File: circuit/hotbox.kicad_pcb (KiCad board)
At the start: 2 copper layers, 59.7 x 26.7 mm, 35 parts, among them IC1 M48, K1 CONN_3, P1 CONN_2, P2 CONN_5, P3 CONN_4, P4 CONN_3X2, U1 REG, U2 OPTO-TRIAC, U3 BTA312Y-600C, U4 OPTO-TRANS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

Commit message: Alpha version of complete pcb, untested.
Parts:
- added 1PIN: P***, Connect:1pin, F.Cu at (87.6, 151.8)
- added 1PIN: P***, Connect:1pin, F.Cu at (139.1, 158.8)
- added 1PIN: P***, Connect:1pin, F.Cu at (139.1, 137.8)
- moved D1 3.81 mm to (85.7, 156.2)
- moved D2 2.54 mm to (85.7, 158.1)
- moved R5 2.54 mm to (92.1, 151.8), turned to 90 degrees
- moved R12 1.91 mm to (89.5, 160.0)
- moved D4 1.27 mm to (85.7, 160.0)
- moved R6 1.27 mm to (89.5, 156.2)
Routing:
- net Net-(D1-Pad1): track 2.32 -> 7.47 mm
- net /load: track 26.2 -> 21.9 mm
- net GND: track 149.3 -> 147.5 mm, vias 13 -> 12
- net Net-(IC1-Pad9): track 25.6 -> 24.3 mm
- net Net-(IC1-Pad1): track 16.7 -> 15.4 mm
- net Net-(D4-Pad1): track 2.32 -> 3.33 mm
- net +3.3V: track 90.9 -> 91.6 mm
- net Net-(D2-Pad1): track 2.32 -> 2.85 mm
- added copper zone on F.Cu, net GND
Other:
- board size 59.7 x 26.7 mm -> 59.7 x 27.7 mm
- board text added: "Hotbox v1.0 J. Villemaire-Krajden http://j-vk.com"

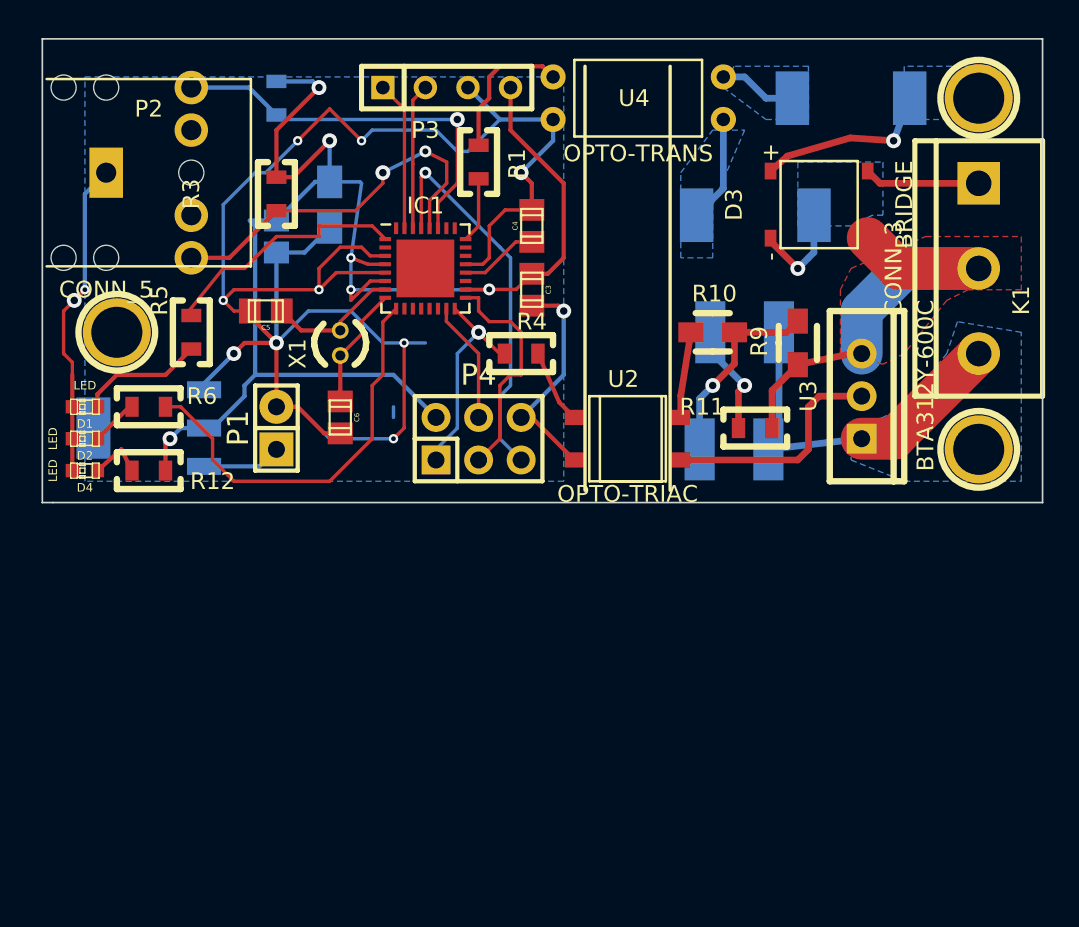
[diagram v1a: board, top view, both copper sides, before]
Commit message: Switched to 5x5cm for seeedstudio.
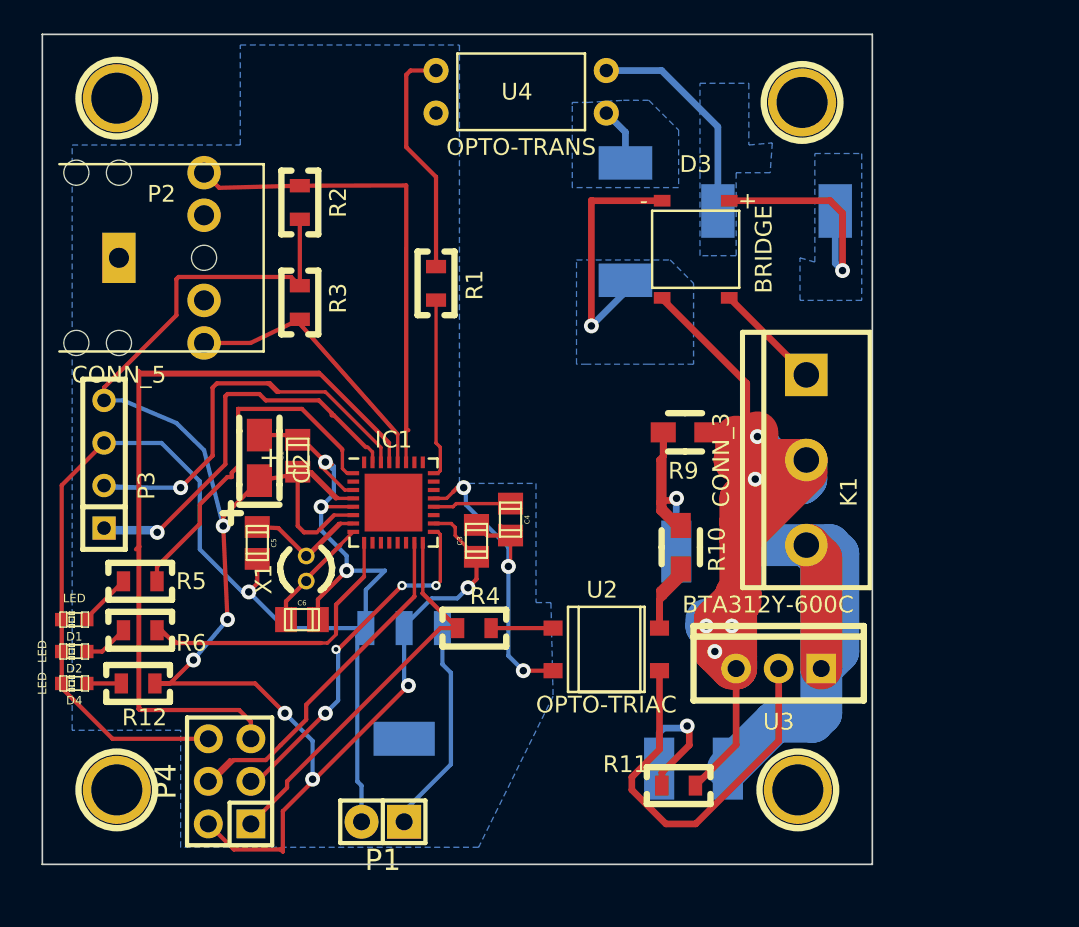
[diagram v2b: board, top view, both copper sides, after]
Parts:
- added 1PIN: P***, Connect:1pin, F.Cu at (128.5, 138.0)
- C1, C2, R2: moved to F.Cu
- moved 1PIN 65.9 mm to (87.6, 179.1)
- moved P3 30.4 mm to (86.9, 159.6), turned to 90 degrees
- moved C8 26.2 mm to (122.0, 177.8)
- moved P4 25.3 mm to (94.4, 178.6), turned to 90 degrees
- moved P1 24.3 mm to (103.5, 181.0), turned to 180 degrees
- moved 1PIN 23.0 mm to (128.3, 179.1)
- moved R11 21.8 mm to (121.2, 178.8)
- moved U1 21.6 mm to (104.8, 172.7), turned to 0 degrees
- moved C4 17.6 mm to (111.1, 162.9), turned to 270 degrees
- moved U3 17.0 mm to (127.1, 171.8), turned to 90 degrees
- moved R4 16.6 mm to (109.0, 169.4)
- moved C2 15.7 mm to (96.1, 159.3), turned to 90 degrees
- moved K1 15.4 mm to (128.8, 159.4)
- moved C3 15.3 mm to (109.1, 164.2), turned to 90 degrees
- moved R5 15.2 mm to (89.0, 166.6), turned to 0 degrees
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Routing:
- net Net-(IC1-Pad29): track 23.5 -> 91.7 mm, vias 1 -> 0
- net /live: track 26.2 -> 86.4 mm, vias 0 -> 5
- net GND: track 147.5 -> 116.6 mm, vias 12 -> 7
- net Net-(IC1-Pad15): track 7.29 -> 36.7 mm
- net Net-(IC1-Pad30): track 8.71 -> 32.7 mm, vias 0 -> 1
- net Net-(IC1-Pad31): track 8.93 -> 30.1 mm, vias 0 -> 1
- net /TH1: track 23.6 -> 44.0 mm, vias 1 -> 0
- net +3.3V: track 91.6 -> 109.7 mm, vias 6 -> 7
- net /load: track 21.9 -> 38.4 mm
- net Net-(IC1-Pad16): track 12.8 -> 26.3 mm, vias 1 -> 0
- net Net-(U2-Pad4): track 13.9 -> 23.8 mm
- net Net-(D3-Pad1): track 6.06 -> 15.3 mm
- net Net-(R7-Pad2): track 4.65 -> 13.1 mm
- net Net-(P1-Pad1): track 4.74 -> 12.9 mm
- net Net-(IC1-Pad17): track 14.3 -> 21.5 mm, vias 0 -> 4
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- removed copper zone on F.Cu, net /live
- removed copper zone on B.Cu, net /load
- removed copper zone on F.Cu, net GND
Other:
- board size 59.7 x 27.7 mm -> 49.5 x 49.5 mm
- board text added: "Hotbox v0.9.1-alpha Auth: Jonathan Villemaire-Krajden http://j-vk.com"
- board text removed: "Hotbox v1.0 J. Villemaire-Krajden http://j-vk.com"

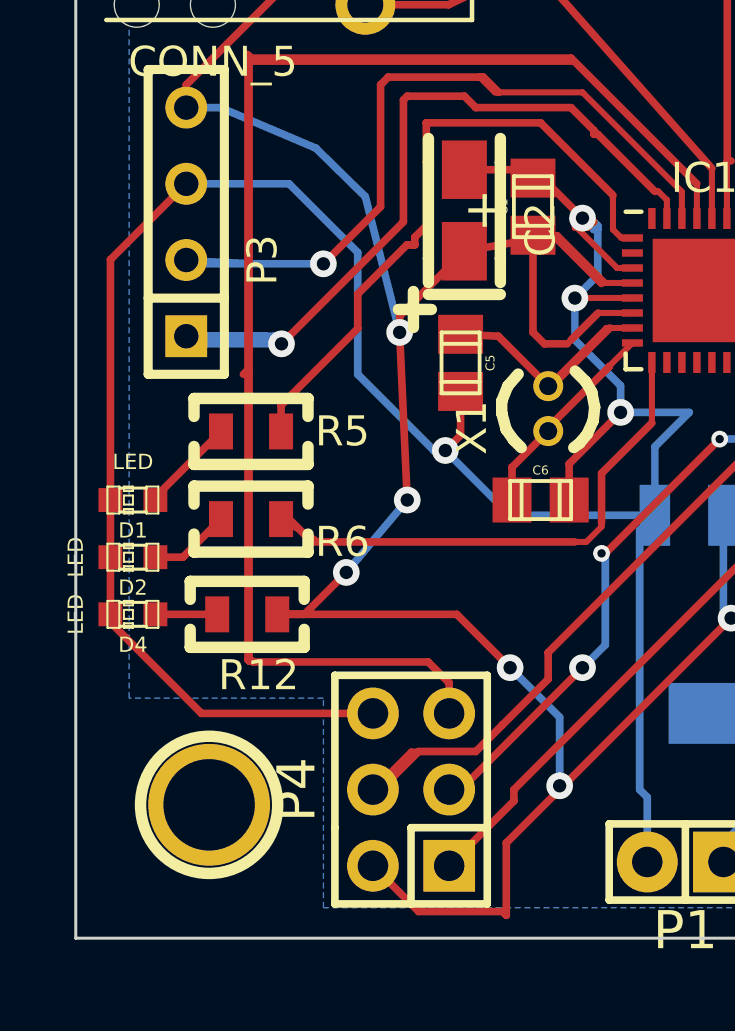
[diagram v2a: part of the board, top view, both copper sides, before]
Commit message: Move traces further from edges.
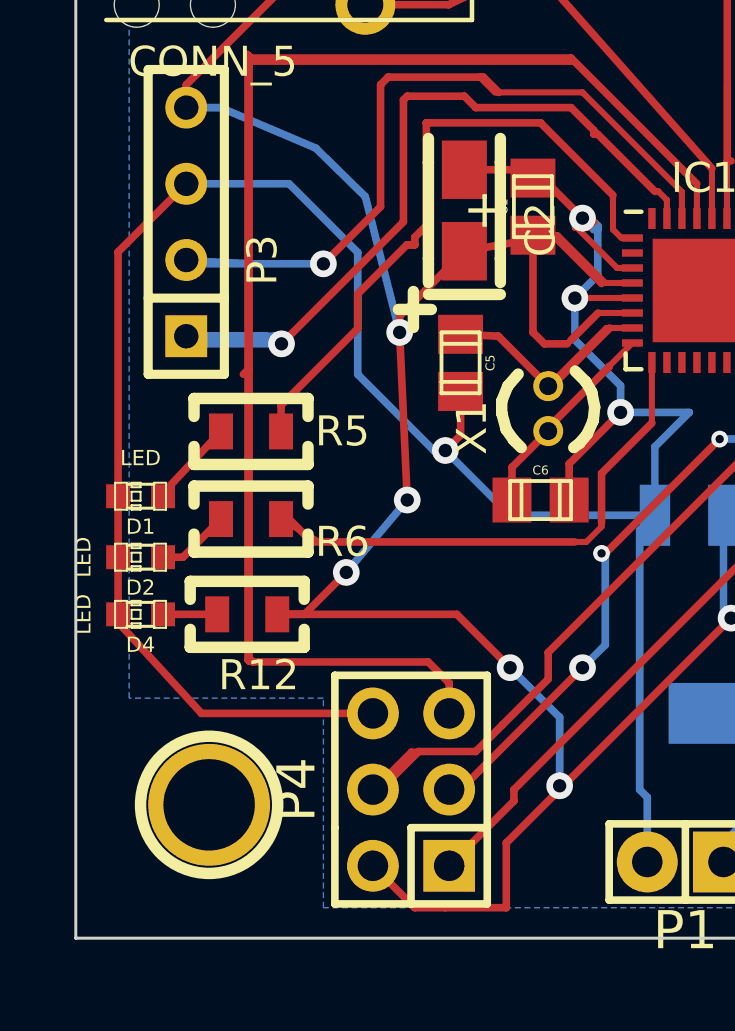
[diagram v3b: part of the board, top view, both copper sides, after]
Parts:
- moved D1 0.28 mm to (85.3, 168.8)
- moved D2 0.25 mm to (85.3, 170.8)
- moved D4 0.25 mm to (85.3, 172.7)

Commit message: 5x5cm version.
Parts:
- removed R12, R5, R6: R, Resistors_SMD:Resistor_SMD0805_ReflowWave
- added RP1: 82R, Resistors_SMD:r_cat16-4, F.Cu at (89.0, 173.0)
- C1, R2, R3, R4, U2: moved to B.Cu
- C2: value CP1 -> 220uF; footprint Capacitors_Tantalum_SMD:TantalC_SizeA_EIA-3216_Reflow -> Capacitors_Tantalum_SMD:TantalC_SizeC_EIA-6032_Reflow
- C3: value C -> 220uF; moved to B.Cu
- C4: value C -> 0.1uF
- C5, C6: value C -> 12pF; moved to B.Cu
- C7: moved to F.Cu
- D1: value LED -> LED-orange
- D2: value LED -> LED-green
- D4: value LED -> LED-blue
- IC1: value M48 -> ATMEGA48A-M
- R10: value R -> 330R
- U1: value REG -> NCP1117ST33T3G; moved to F.Cu
- U4: value OPTO-TRANS -> OPTO-TRANSISTOR4
- moved U4 41.9 mm to (110.2, 179.3), turned to 180 degrees
- moved R7 34.2 mm to (119.6, 177.9), turned to 270 degrees
- moved R1 32.5 mm to (101.6, 181.0), turned to 180 degrees
- moved P1 32.1 mm to (94.6, 150.1)
- moved D3 29.2 mm to (121.2, 176.0), turned to 90 degrees
- moved R11 28.7 mm to (116.5, 150.5), turned to 180 degrees
- moved C8 27.4 mm to (119.9, 150.5)
- moved R8 26.6 mm to (114.6, 171.6), turned to 270 degrees
- moved C2 22.1 mm to (94.9, 181.4), turned to 180 degrees
- moved C3 16.6 mm to (96.0, 174.5)
- moved U1 16.6 mm to (100.7, 156.6)
- moved U2 15.1 mm to (110.4, 157.1)
- moved P4 14.4 mm to (105.0, 168.9), turned to 270 degrees
- moved P2 12.5 mm to (89.7, 159.8)
- moved X1 12.0 mm to (99.7, 177.8), turned to 0 degrees
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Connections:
- IC1 pad 11: Net-(IC1-Pad11) -> /zc
- K1 pad 1: /neutral -> /live
- K1 pad 2: /live -> /load
- K1 pad 3: /load -> /neutral
- R1 pad 1: Net-(R1-Pad1) -> /zc
- R1 pad 2: Net-(IC1-Pad24) -> +3.3V
- U4 pad 1: Net-(R1-Pad1) -> Net-(R7-Pad2)
- U4 pad 2: GND -> Net-(R8-Pad2)
- U4 pad 3: Net-(R8-Pad2) -> GND
- U4 pad 4: Net-(R7-Pad2) -> /zc
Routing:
- net Net-(IC1-Pad29): track 91.7 -> 25.0 mm, vias 0 -> 2
- net GND: track 116.4 -> 57.4 mm, vias 7 -> 10
- net Net-(IC1-Pad9): track 29.8 -> 0.00 mm
- net Net-(IC1-Pad15): track 36.7 -> 7.42 mm
- net Net-(IC1-Pad30): track 32.7 -> 9.83 mm, vias 1 -> 0
- net /TH1: track 44.0 -> 21.3 mm
- net Net-(IC1-Pad16): track 26.3 -> 8.63 mm
- net Net-(IC1-Pad31): track 30.1 -> 13.0 mm, vias 1 -> 0
- net +3.3V: track 109.4 -> 93.8 mm
- net /zc: track 0.00 -> 15.3 mm, vias 0 -> 2
- net Net-(IC1-Pad1): track 22.0 -> 7.57 mm
- net Net-(R1-Pad1): track 14.1 -> 0.00 mm
- net /live: track 86.4 -> 73.0 mm, vias 5 -> 0
- net Net-(D3-Pad1): track 15.3 -> 28.4 mm
- net Net-(U2-Pad4): track 23.8 -> 11.5 mm
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- added copper zone on F.Cu, net /live
- added copper zone on B.Cu, net /load
- added copper zone on F.Cu, net GND
- removed copper zone on B.Cu, net Net-(D3-Pad1)
- removed copper zone on B.Cu, net Net-(D3-Pad3)
- removed copper zone on B.Cu, net Net-(R7-Pad2)
- removed copper zone on B.Cu, net Net-(R8-Pad2)
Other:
- rule via_min_drill: 0.3556 -> 0.3
- rule via_min_size: 0.5588 -> 0.508

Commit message: Simplifid schematics removed snubber circuit (not necessary with BTA312Y).
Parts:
- removed C7, C8: C, Capacitors_SMD:c_1812
- removed R11: R, Resistors_SMD:Resistor_SMD0805_ReflowWave
- removed R9: R, Resistors_SMD:Resistor_SMD0805_HandSoldering
- R10: footprint Resistors_SMD:Resistor_SMD0805_HandSoldering -> Resistors_SMD:R_0805
- U4: value OPTO-TRANSISTOR4 -> PC123
- moved D3 3.97 mm to (120.7, 172.1)
- moved U2 2.80 mm to (110.5, 154.3)
- moved U3 2.68 mm to (120.7, 159.4)
- moved R7 2.27 mm to (120.7, 175.9)
- moved R10 1.08 mm to (114.3, 159.4)
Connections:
- net +3.3V renamed +3V3
- R10 pad 2: Net-(C7-Pad2) -> /live
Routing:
- net /live: track 73.0 -> 50.4 mm
- net Net-(D3-Pad1): track 28.4 -> 13.5 mm
- net /load: track 45.8 -> 32.4 mm
- net Net-(C7-Pad2): track 9.49 -> 0.00 mm
- net Net-(C8-Pad2): track 6.36 -> 0.00 mm, vias 1 -> 0
- net Net-(R10-Pad1): track 10.4 -> 4.47 mm
- net /neutral: track 10.0 -> 6.43 mm
- net Net-(R4-Pad1): track 4.43 -> 6.86 mm
- net GND: track 57.4 -> 59.1 mm
- net Net-(R7-Pad2): track 4.66 -> 5.51 mm
- net Net-(D3-Pad3): track 6.35 -> 6.90 mm
- removed copper zone on F.Cu, net /live
- removed copper zone on B.Cu, net /load
